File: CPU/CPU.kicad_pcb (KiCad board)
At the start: 4 copper layers, 364 x 203 mm, 335 parts, among them J1 Conn_02x36_Top_Bottom, P2 Conn_02x13_Top_Bottom, P3 Conn_02x13_Top_Bottom, P4 IDC-16, P5 Conn_02x25_Counter_Clockwise, P6 Conn_02x25_Counter_Clockwise, P7 Conn_02x07_Counter_Clockwise, P8 Conn_02x08_Odd_Even

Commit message: Some track rearrangement
Relax some tight places for ease of soldering
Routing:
- net /Sys.~{D_{2}}: track 40.3 -> 41.5 mm
- net DataP.D_{2}: track 630.1 -> 631.2 mm
- net /PTR.Q_{4}: track 164.0 -> 165.1 mm
- net DataF.D_{2}: track 419.4 -> 420.4 mm
- net /PTR.Q_{5}: track 157.5 -> 158.4 mm

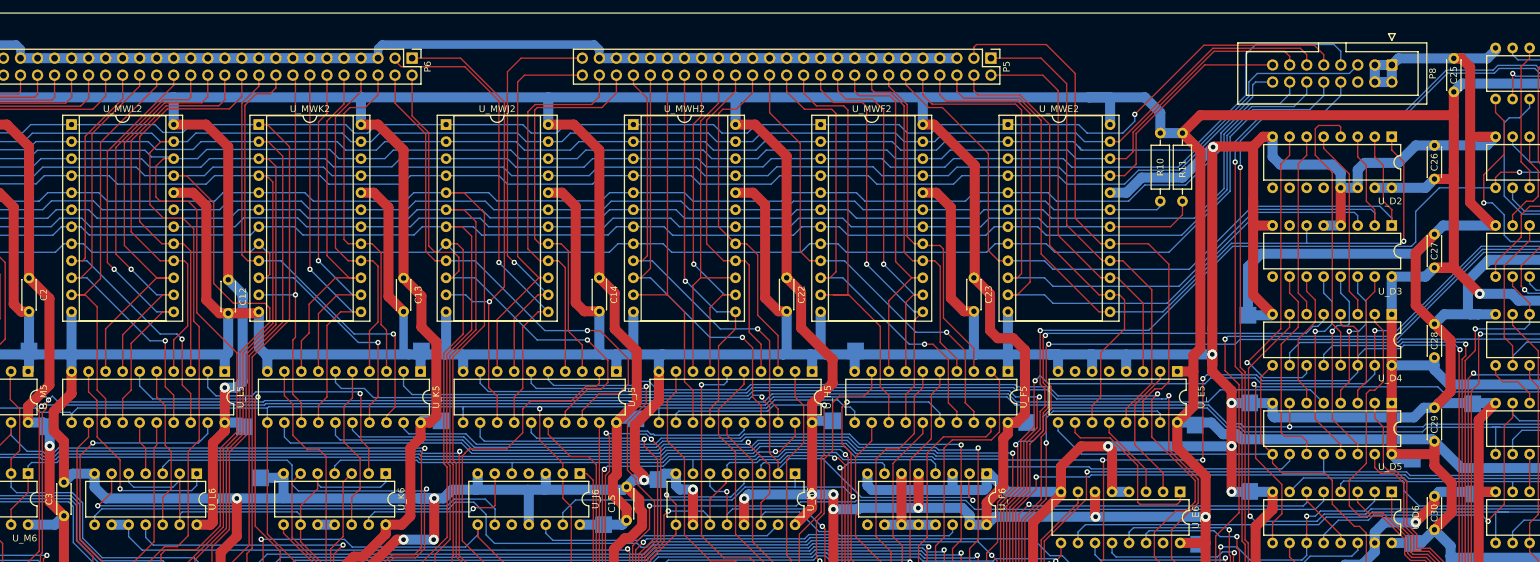
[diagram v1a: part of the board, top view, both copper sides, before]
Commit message: CPU: Improve uROM debugging
Bring back uROM disable on P8 pin 6. This may be handy for testing the board.
Also provide +5V on the connector. During debugging we may want to force 1 on
certain MW lines, so +5V on the debug connector may be handy for that.
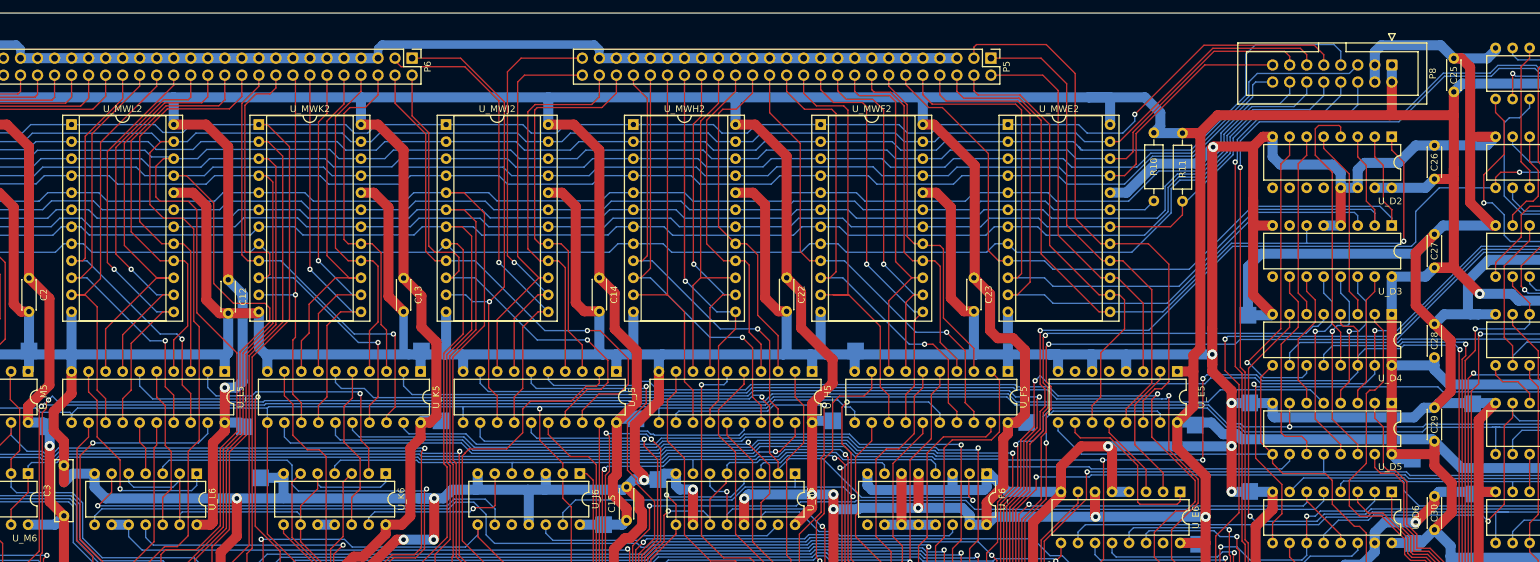
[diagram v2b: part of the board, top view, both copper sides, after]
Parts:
- C3: footprint Capacitor_THT:C_Disc_D4.3mm_W1.9mm_P5.00mm -> Capacitor_THT:C_Rect_L9.0mm_W2.5mm_P7.50mm_MKT
- moved R10 0.97 mm to (232.7, 41.9)
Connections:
- P8 pad 1: GND -> +5V
- P8 pad 2: GND -> +5V
- P8 pad 6: unconnected-(P8-Pad6) -> Net-(R11-Pad2)
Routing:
- net Net-(R11-Pad2): track 187.6 -> 224.5 mm
- net +5V: track 4583.0 -> 4593.4 mm
- net GND: track 5034.4 -> 5032.1 mm
- net Net-(R10-Pad2): track 182.5 -> 181.1 mm
- net MWS.A_{1}: track 311.6 -> 310.4 mm
- net MWS.A_{2}: track 310.1 -> 308.9 mm
- net MWS.A_{0}: track 312.3 -> 311.1 mm

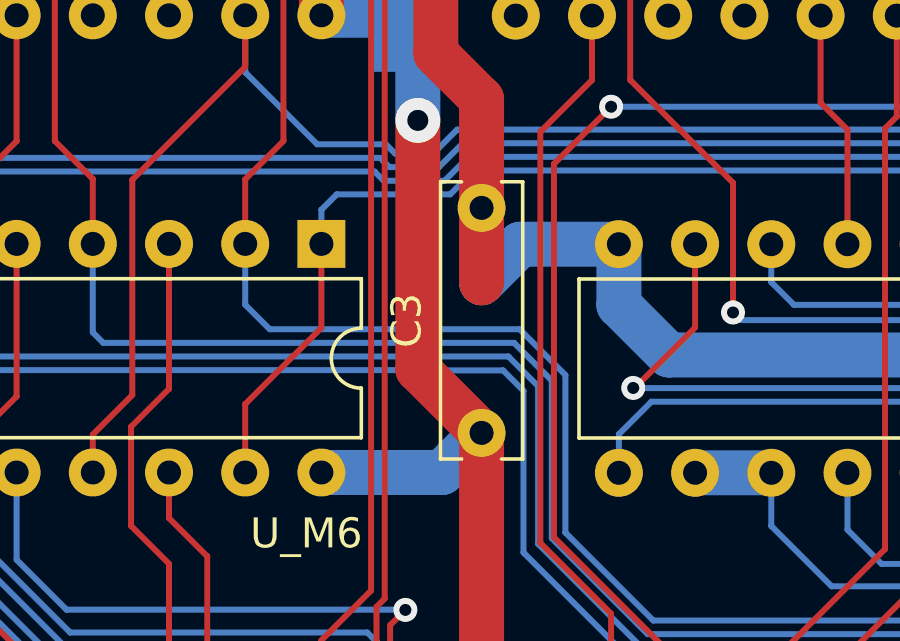
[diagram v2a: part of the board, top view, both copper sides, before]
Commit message: CPU: Fix C3 footprint
Fix broken footprint (forgot to update footprints in the SCH)
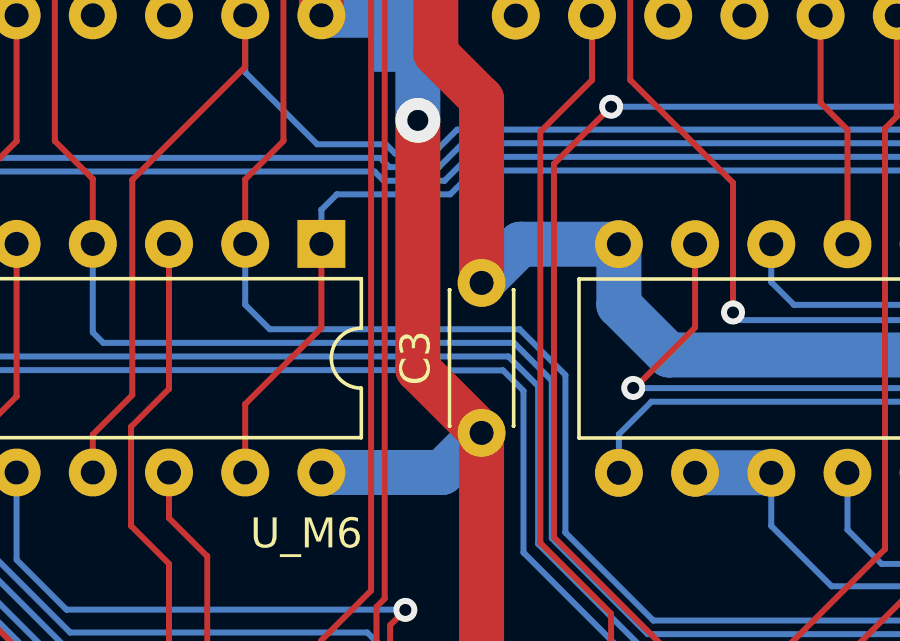
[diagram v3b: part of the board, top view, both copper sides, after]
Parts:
- C3: footprint Capacitor_THT:C_Rect_L9.0mm_W2.5mm_P7.50mm_MKT -> Capacitor_THT:C_Disc_D4.3mm_W1.9mm_P5.00mm
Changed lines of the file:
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@@
     )
   )
-  (footprint "Capacitor_THT:C_Rect_L9.0mm_W2.5mm_P7.50mm_MKT" (layer "F.Cu")
+  (footprint "Capacitor_THT:C_Disc_D4.3mm_W1.9mm_P5.00mm" (layer "F.Cu")
     (at 70.104 99.01 90)
-    (descr "C, Rect series, Radial, pin pitch=7.50mm, , length*width=9*2.5mm^2, Capacitor, https://en.tdk.eu/inf/20/20/db/fc_2009/MKT_B32560_564.pdf")
-    (tags "C Rect series Radial pin pitch 7.50mm  length 9mm width 2.5mm Capacitor")
+    (descr "C, Disc series, Radial, pin pitch=5.00mm, , diameter*width=4.3*1.9mm^2, Capacitor, http://www.vishay.com/docs/45233/krseries.pdf")
+    (tags "C Disc series Radial pin pitch 5.00mm  diameter 4.3mm width 1.9mm Capacitor")
     (property "Sheetfile" "CPU.kicad_sch")
     (property "Sheetname" "")
     (attr through_hole)
-    (fp_text reference "C3" (at 3.75 -2.5 90) (layer "F.SilkS")
+    (fp_text reference "C3" (at 2.5 -2.2 90) (layer "F.SilkS")
       (effects (font (size 1 1) (thickness 0.15)))
     )
-    (fp_text value "100nF" (at 3.75 2.5 90) (layer "F.Fab")
+    (fp_text value "100nF" (at 2.5 2.2 90) (layer "F.Fab")
       (effects (font (size 1 1) (thickness 0.15)))
     )
-    (fp_text user "${REFERENCE}" (at 3.75 0 90) (layer "F.Fab")
-      (effects (font (size 1 1) (thickness 0.15)))
+    (fp_text user "${REFERENCE}" (at 2.5 0 90) (layer "F.Fab")
+      (effects (font (size 0.86 0.86) (thickness 0.129)))
     )
-    (fp_line (start 8.37 -1.37) (end 8.37 -0.665) (layer "F.SilkS") (width 0.12))
-    (fp_line (start -0.87 0.665) (end -0.87 1.37) (layer "F.SilkS") (width 0.12))
-    (fp_line (start -0.87 1.37) (end 8.37 1.37) (layer "F.SilkS") (width 0.12))
-    (fp_line (start -0.87 -1.37) (end 8.37 -1.37) (layer "F.SilkS") (width 0.12))
-    (fp_line (start -0.87 -1.37) (end -0.87 -0.665) (layer "F.SilkS") (width 0.12))
-    (fp_line (start 8.37 0.665) (end 8.37 1.37) (layer "F.SilkS") (width 0.12))
-    (fp_line (start 8.55 -1.5) (end -1.05 -1.5) (layer "F.CrtYd") (width 0.05))
-    (fp_line (start 8.55 1.5) (end 8.55 -1.5) (layer "F.CrtYd") (width 0.05))
-    (fp_line (start -1.05 -1.5) (end -1.05 1.5) (layer "F.CrtYd") (width 0.05))
-    (fp_line (start -1.05 1.5) (end 8.55 1.5) (layer "F.CrtYd") (width 0.05))
-    (fp_line (start -0.75 -1.25) (end -0.75 1.25) (layer "F.Fab") (width 0.1))
-    (fp_line (start 8.25 -1.25) (end -0.75 -1.25) (layer "F.Fab") (width 0.1))
-    (fp_line (start 8.25 1.25) (end 8.25 -1.25) (layer "F.Fab") (width 0.1))
-    (fp_line (start -0.75 1.25) (end 8.25 1.25) (layer "F.Fab") (width 0.1))
+    (fp_line (start 0.23 1.055) (end 0.23 1.07) (layer "F.SilkS") (width 0.12))
+    (fp_line (start 4.77 -1.07) (end 4.77 -1.055) (layer "F.SilkS") (width 0.12))
+    (fp_line (start 0.23 -1.07) (end 4.77 -1.07) (layer "F.SilkS") (width 0.12))
+    (fp_line (start 0.23 1.07) (end 4.77 1.07) (layer "F.SilkS") (width 0.12))
+    (fp_line (start 0.23 -1.07) (end 0.23 -1.055) (layer "F.SilkS") (width 0.12))
+    (fp_line (start 4.77 1.055) (end 4.77 1.07) (layer "F.SilkS") (width 0.12))
+    (fp_line (start -1.05 1.2) (end 6.05 1.2) (layer "F.CrtYd") (width 0.05))
+    (fp_line (start 6.05 -1.2) (end -1.05 -1.2) (layer "F.CrtYd") (width 0.05))
+    (fp_line (start -1.05 -1.2) (end -1.05 1.2) (layer "F.CrtYd") (width 0.05))
+    (fp_line (start 6.05 1.2) (end 6.05 -1.2) (layer "F.CrtYd") (width 0.05))
+    (fp_line (start 4.65 0.95) (end 4.65 -0.95) (layer "F.Fab") (width 0.1))
+    (fp_line (start 0.35 0.95) (end 4.65 0.95) (layer "F.Fab") (width 0.1))
+    (fp_line (start 0.35 -0.95) (end 0.35 0.95) (layer "F.Fab") (width 0.1))
+    (fp_line (start 4.65 -0.95) (end 0.35 -0.95) (layer "F.Fab") (width 0.1))
     (pad "1" thru_hole circle (at 0 0 90) (size 1.6 1.6) (drill 0.8) (layers *.Cu *.Mask)
       (net 7 "+5V") (pintype "passive"))
-    (pad "2" thru_hole circle (at 7.5 0 90) (size 1.6 1.6) (drill 0.8) (layers *.Cu *.Mask)
+    (pad "2" thru_hole circle (at 5 0 90) (size 1.6 1.6) (drill 0.8) (layers *.Cu *.Mask)
       (net 25 "GND") (pintype "passive"))
-    (model "${KICAD6_3DMODEL_DIR}/Capacitor_THT.3dshapes/C_Rect_L9.0mm_W2.5mm_P7.50mm_MKT.wrl"
+    (model "${KICAD6_3DMODEL_DIR}/Capacitor_THT.3dshapes/C_Disc_D4.3mm_W1.9mm_P5.00mm.wrl"
       (offset (xyz 0 0 0))
       (scale (xyz 1 1 1))
